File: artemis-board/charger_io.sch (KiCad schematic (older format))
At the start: 5 parts, among them J3 USB_B_Micro, J4 Solar in, U15 IP4220CZ6

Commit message: fixed erc
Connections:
- no-connect marks 2 -> 4
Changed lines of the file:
@@
 $Descr A4 11693 8268
 encoding utf-8
-Sheet 7 6
+Sheet 6 6
 Title "SuperPower-uC"
 Date "2020-09-20"
@@
 Wire Wire Line
 	4400 4550 4700 4550
+NoConn ~ 4400 4650
+NoConn ~ 3550 4650
 $EndSCHEMATC

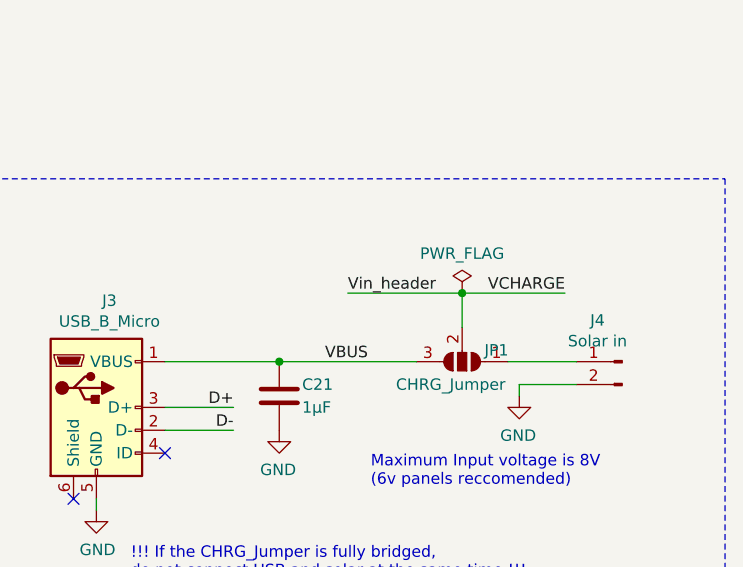
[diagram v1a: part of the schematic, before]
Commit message: removed unused net label
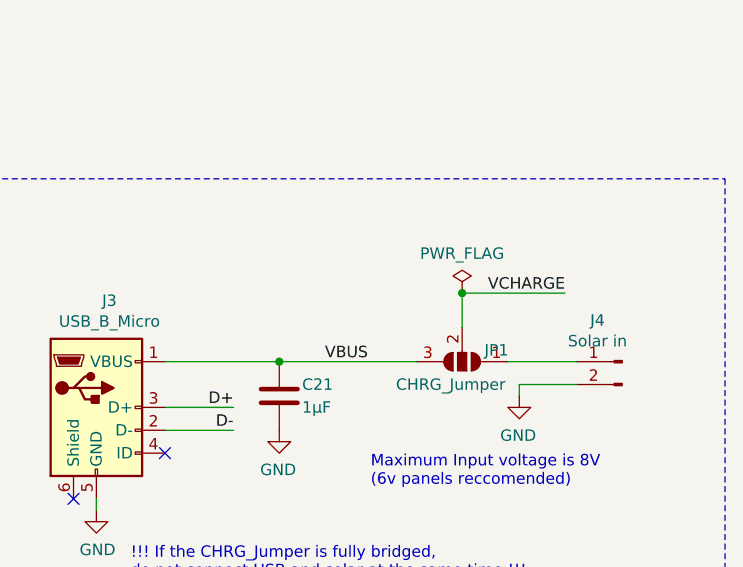
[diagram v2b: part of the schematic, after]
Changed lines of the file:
@@
 Text Notes 600  650  0    50   ~ 0
 Labels\n
-Text Label 4400 2700 0    50   ~ 0
-Vin_header
-Wire Wire Line
-	4400 2700 4900 2700
 Wire Wire Line
 	3300 3600 3300 3650

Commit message: moved R8 and did some minor silk and routing changes
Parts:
- J3: LCSC C319164 -> C404969
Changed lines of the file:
@@
 F 1 "USB_B_Micro" H 3357 3576 50  0000 C CNN
 F 2 "Connector_USB:USB_Micro-B_Molex-105017-0001" H 3357 3575 50  0001 C CNN
-F 3 "https://datasheet.lcsc.com/szlcsc/2002271812_XKB-Connectivity-U254-051T-4BH23-S2B_C319164.pdf" H 3450 3150 50  0001 C CNN
-F 4 "C319164" H 3300 3200 50  0001 C CNN "LCSC"
+F 3 "https://datasheet.lcsc.com/szlcsc/1912111437_SHOU-HAN-MicroXNJ_C404969.pdf" H 3450 3150 50  0001 C CNN
+F 4 "C404969" H 3300 3200 50  0001 C CNN "LCSC"
 	1    3300 3200
 	1    0    0    -1

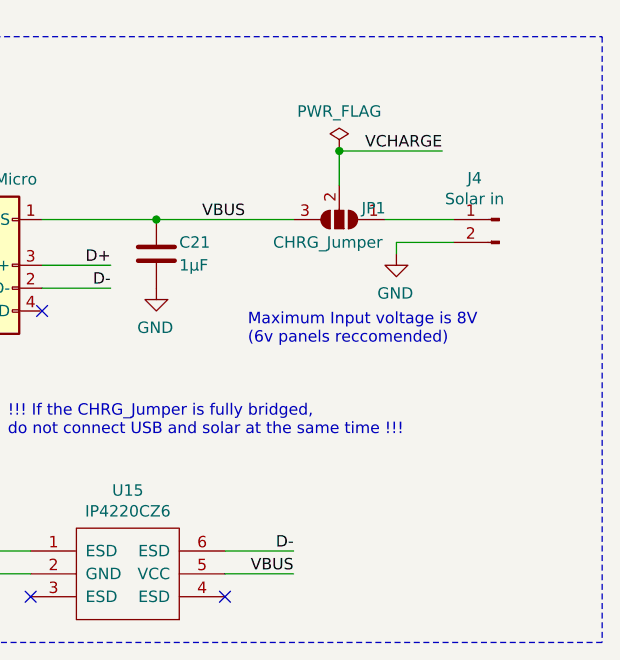
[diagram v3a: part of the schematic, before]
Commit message: added comments and swapped polarity of Vin connector
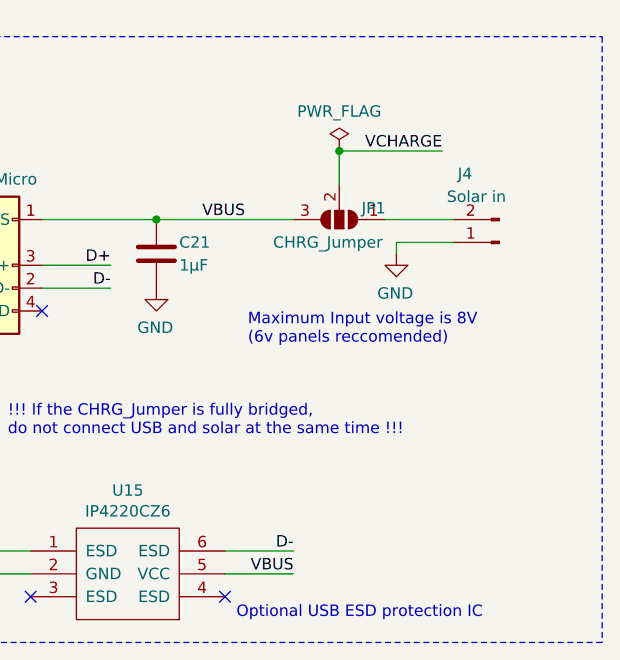
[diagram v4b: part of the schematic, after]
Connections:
- net GND: now also J4.1 (Pin_1); no longer J4.2 (Pin_2)
- net at JP1.1 (A): now also J4.2 (Pin_2); no longer J4.1 (Pin_1)
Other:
- note added: "Optional USB ESD protection IC"
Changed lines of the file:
@@
 L Connector:Conn_01x02_Male J4
 U 1 1 5F7CE401
-P 5600 3000
-F 0 "J4" H 5708 3181 50  0000 C CNN
-F 1 "Solar in" H 5708 3090 50  0000 C CNN
-F 2 "Connector_JST:JST_EH_S2B-EH_1x02_P2.50mm_Horizontal" H 5600 3000 50  0001 C CNN
-F 3 "https://datasheet.lcsc.com/szlcsc/1811051822_JST-Sales-America-S2B-XH-A-LF-SN_C157931.pdf" H 5600 3000 50  0001 C CNN
-F 4 "C157931" H 5600 3000 50  0001 C CNN "LCSC"
-	1    5600 3000
-	-1   0    0    -1
+P 5600 3100
+F 0 "J4" H 5750 2800 50  0000 C CNN
+F 1 "Solar in" H 5700 2900 50  0000 C CNN
+F 2 "Connector_JST:JST_EH_S2B-EH_1x02_P2.50mm_Horizontal" H 5600 3100 50  0001 C CNN
+F 3 "https://datasheet.lcsc.com/szlcsc/1811051822_JST-Sales-America-S2B-XH-A-LF-SN_C157931.pdf" H 5600 3100 50  0001 C CNN
+F 4 "C157931" H 5600 3100 50  0001 C CNN "LCSC"
+	1    5600 3100
+	-1   0    0    1
 $EndComp
 $Comp
@@
 NoConn ~ 4400 4650
 NoConn ~ 3550 4650
+Text Notes 4450 4750 0    50   ~ 0
+Optional USB ESD protection IC
 $EndSCHEMATC

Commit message: swapped and added some lcsc part numbers and DNP markers
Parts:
- C21: footprint Capacitor_SMD:C_0603_1608Metric_Pad1.05x0.95mm_HandSolder -> Capacitor_SMD:C_0603_1608Metric_Pad1.08x0.95mm_HandSolder
- J4: LCSC C157931 -> C225424
- JP1: DNP (none) -> DNP
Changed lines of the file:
@@
 F 2 "Connector_JST:JST_EH_S2B-EH_1x02_P2.50mm_Horizontal" H 5600 3100 50  0001 C CNN
 F 3 "https://datasheet.lcsc.com/szlcsc/1811051822_JST-Sales-America-S2B-XH-A-LF-SN_C157931.pdf" H 5600 3100 50  0001 C CNN
-F 4 "C157931" H 5600 3100 50  0001 C CNN "LCSC"
+F 4 "C225424" H 5600 3100 50  0001 C CNN "LCSC"
 	1    5600 3100
 	-1   0    0    1
@@
 F 2 "Jumper:SolderJumper-3_P1.3mm_Open_Pad1.0x1.5mm" H 4900 3000 50  0001 C CNN
 F 3 "~" H 4900 3000 50  0001 C CNN
+F 4 "DNP" H 4900 3000 50  0001 C CNN "DNP"
 	1    4900 3000
 	-1   0    0    1
@@
 F 0 "C21" H 4200 3200 50  0000 L CNN
 F 1 "1µF" H 4200 3100 50  0000 L CNN
-F 2 "Capacitor_SMD:C_0603_1608Metric_Pad1.05x0.95mm_HandSolder" H 4138 3000 50  0001 C CNN
+F 2 "Capacitor_SMD:C_0603_1608Metric_Pad1.08x0.95mm_HandSolder" H 4138 3000 50  0001 C CNN
 F 3 "~" H 4100 3150 50  0001 C CNN
 F 4 "C15849" H 4100 3150 50  0001 C CNN "LCSC"

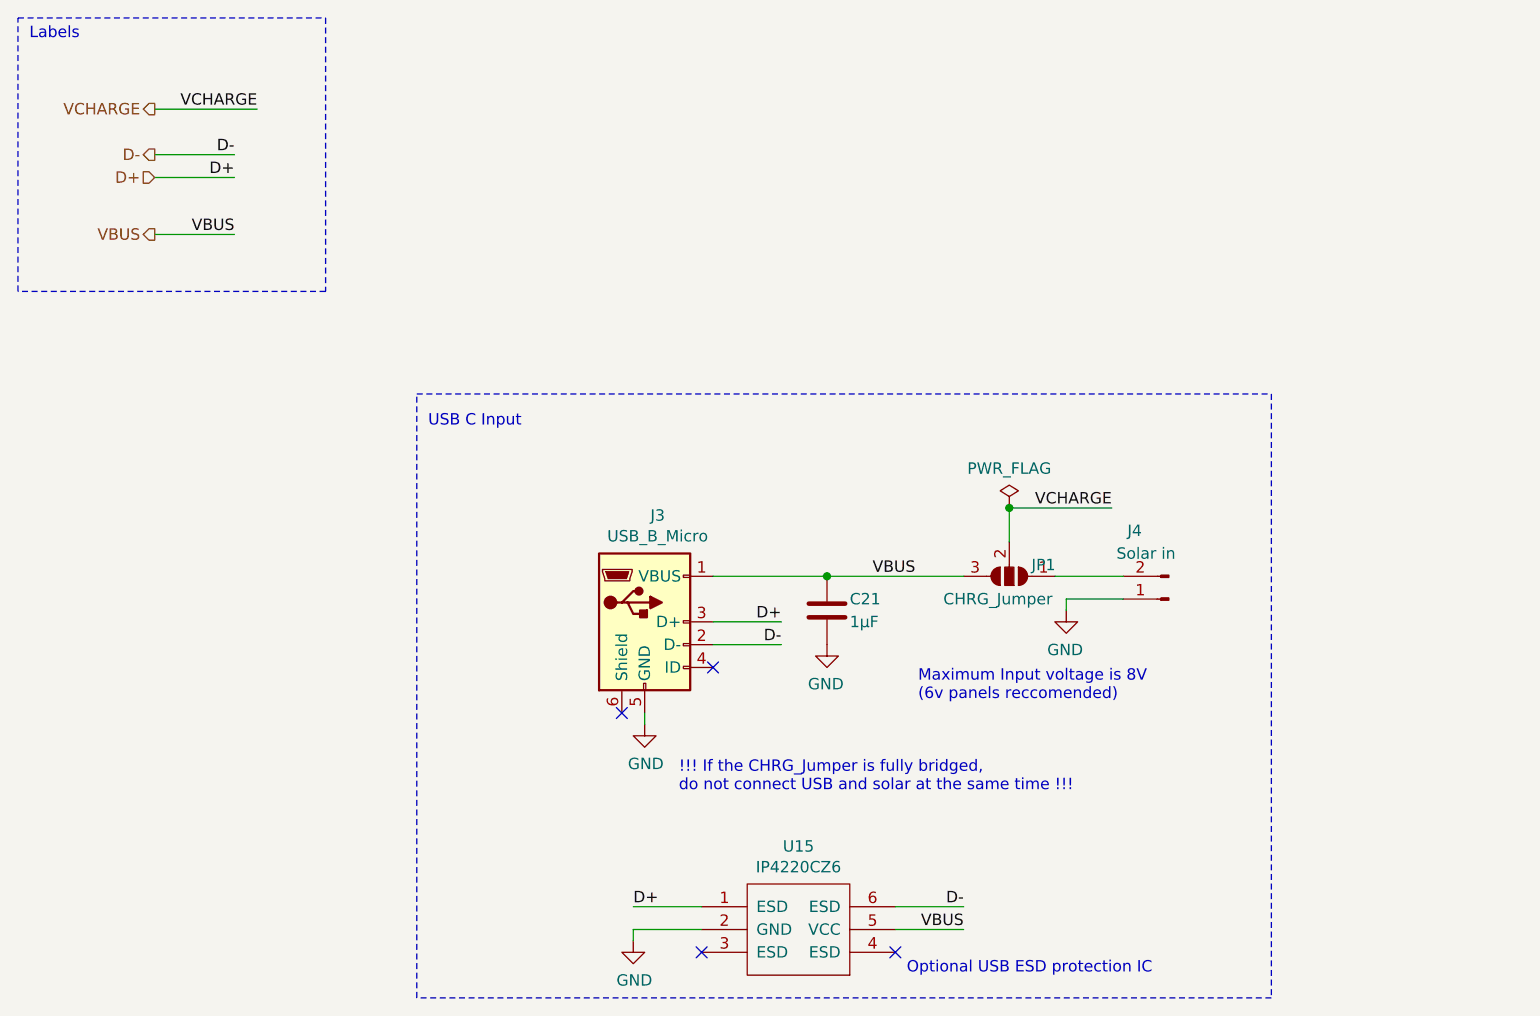
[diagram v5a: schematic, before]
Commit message: added reverse polarity protection to power input
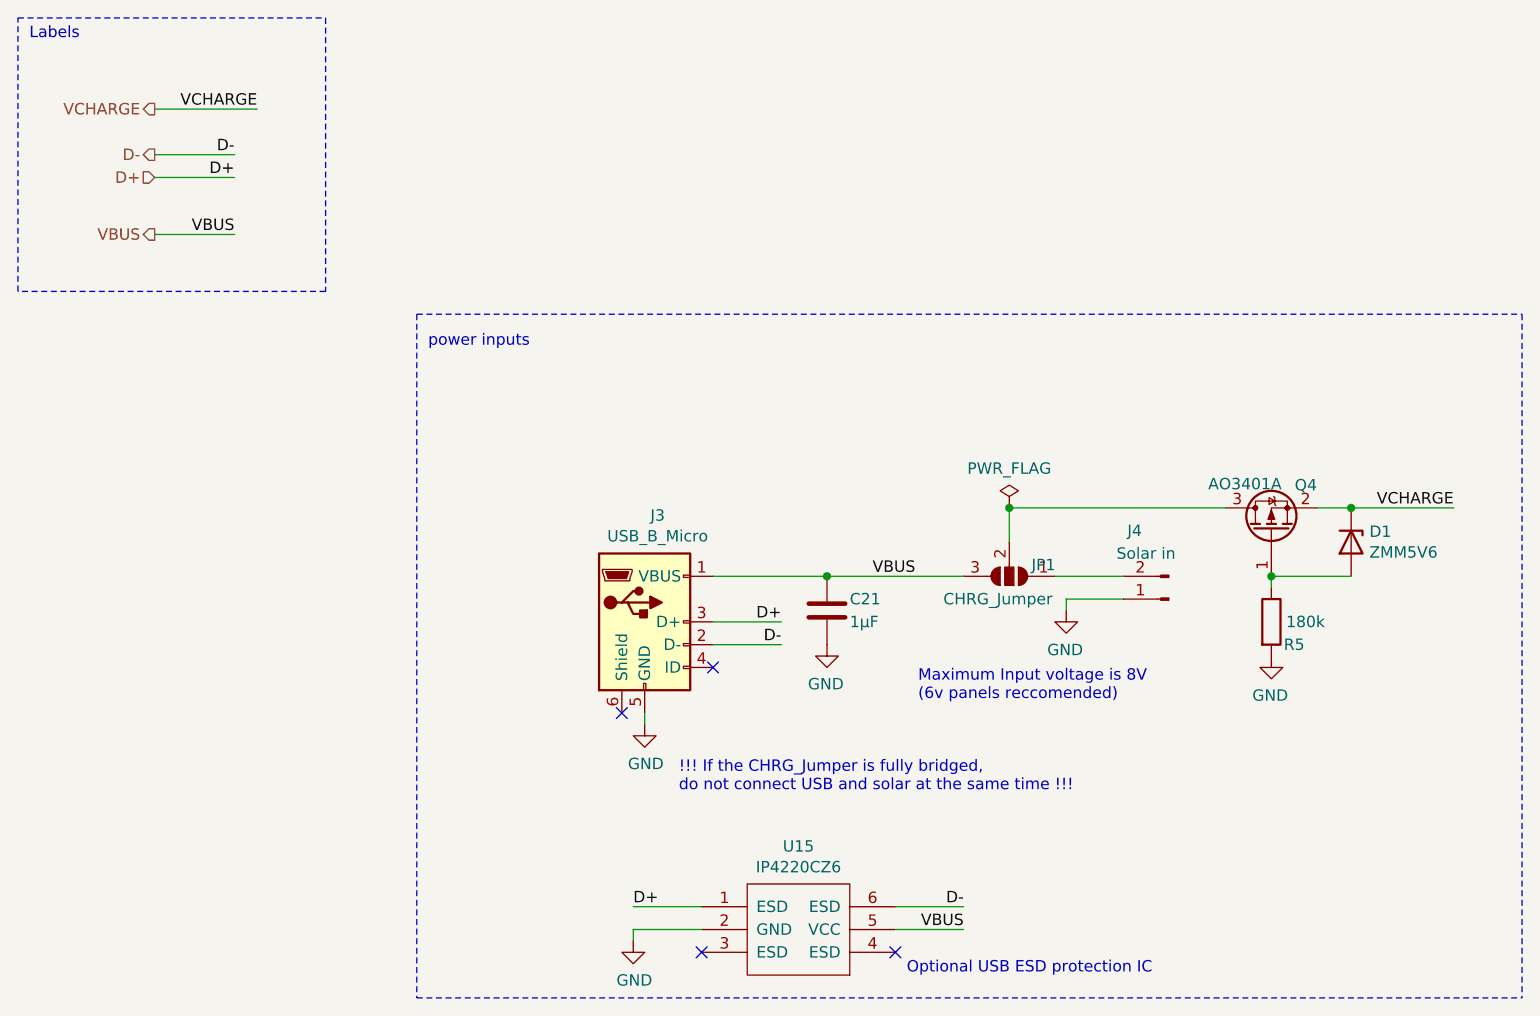
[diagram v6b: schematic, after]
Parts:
- added D1: ZMM5V6, Diode_SMD:D_MiniMELF, symbol Device:D_Zener
- added Q4: AO3401A, Package_TO_SOT_SMD:SOT-23, symbol Transistor_FET:AO3401A
- added R5: 180k, Resistor_SMD:R_0603_1608Metric_Pad1.05x0.95mm_HandSolder, symbol Device:R
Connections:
- net GND: now also R5.2
- net VCHARGE: now also D1.1 (K), Q4.2 (S); no longer JP1.2 (C)
- new net: JP1.2 (C), Q4.3 (D)
- new net: D1.2 (A), Q4.1 (G), R5.1
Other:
- note added: "power inputs\n"
- note removed: "USB C Input\n"
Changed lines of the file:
@@
 Text Label 3900 3300 2    50   ~ 0
 D-
-Wire Notes Line
-	2300 2200 6050 2200
-Wire Notes Line
-	6050 2200 6050 4850
-Wire Notes Line
-	6050 4850 2300 4850
-Wire Notes Line
-	2300 4850 2300 2200
-Text Notes 2350 2350 0    50   ~ 0
-USB C Input\n
+Text Notes 2350 2000 0    50   ~ 0
+power inputs\n
 Text HLabel 1150 950  0    50   Output ~ 0
 VCHARGE
@@
 Text Label 1500 1500 2    50   ~ 0
 VBUS
-Text Label 5350 2700 2    50   ~ 0
+Text Label 6850 2700 2    50   ~ 0
 VCHARGE
-Wire Wire Line
-	4900 2700 5350 2700
 Wire Notes Line
 	550  550  1900 550
@@
 Text Notes 4450 4750 0    50   ~ 0
 Optional USB ESD protection IC
+$Comp
+L Transistor_FET:AO3401A Q?
+U 1 1 61186A66
+P 6050 2800
+AR Path="/5F63A0E9/61186A66" Ref="Q?"  Part="1"
+AR Path="/5F63B107/61186A66" Ref="Q4"  Part="1"
+F 0 "Q4" V 6250 2600 50  0000 L CNN
+F 1 "AO3401A" V 6255 2755 50  0000 L CNN
+F 2 "Package_TO_SOT_SMD:SOT-23" H 6250 2725 50  0001 L CIN
+F 3 "http://www.aosmd.com/pdfs/datasheet/AO3401A.pdf" H 6050 2800 50  0001 L CNN
+F 4 "C15127" H 6050 2800 50  0001 C CNN "LCSC"
+	1    6050 2800
+	0    -1   -1   0
+$EndComp
+Wire Notes Line
+	2300 1850 2300 4850
+Wire Notes Line
+	2300 1850 7150 1850
+Wire Notes Line
+	7150 1850 7150 4850
+Wire Notes Line
+	2300 4850 7150 4850
+Wire Wire Line
+	4900 2700 5850 2700
+Wire Wire Line
+	6250 2700 6400 2700
+Wire Wire Line
+	6050 3000 6050 3050
+$Comp
+L power:GND #PWR?
+U 1 1 6118D6BE
+P 6050 3350
+F 0 "#PWR?" H 6050 3100 50  0001 C CNN
+F 1 "GND" H 6055 3177 50  0000 C CNN
+F 2 "" H 6050 3350 50  0001 C CNN
+F 3 "" H 6050 3350 50  0001 C CNN
+	1    6050 3350
+	-1   0    0    -1
+$EndComp
+$Comp
+L Device:D_Zener D1
+U 1 1 61192259
+P 6400 2850
+F 0 "D1" V 6354 2930 50  0000 L CNN
+F 1 "ZMM5V6" V 6445 2930 50  0000 L CNN
+F 2 "Diode_SMD:D_MiniMELF" H 6400 2850 50  0001 C CNN
+F 3 "~" H 6400 2850 50  0001 C CNN
+F 4 "C8062" V 6400 2850 50  0001 C CNN "LCSC"
+	1    6400 2850
+	0    1    1    0
+$EndComp
+Connection ~ 6400 2700
+Wire Wire Line
+	6400 2700 6850 2700
+Wire Wire Line
+	6400 3000 6050 3000
+Connection ~ 6050 3000
+$Comp
+L Device:R R?
+U 1 1 6119B3B3
+P 6050 3200
+AR Path="/5F63A00B/6119B3B3" Ref="R?"  Part="1"
+AR Path="/5F63B107/6119B3B3" Ref="R5"  Part="1"
+F 0 "R5" H 6150 3100 50  0000 C CNN
+F 1 "180k" H 6200 3200 50  0000 C CNN
+F 2 "Resistor_SMD:R_0603_1608Metric_Pad1.05x0.95mm_HandSolder" V 5980 3200 50  0001 C CNN
+F 3 "~" H 6050 3200 50  0001 C CNN
+F 4 "C22827" H 6050 3200 50  0001 C CNN "LCSC"
+	1    6050 3200
+	1    0    0    -1
+$EndComp
 $EndSCHEMATC
